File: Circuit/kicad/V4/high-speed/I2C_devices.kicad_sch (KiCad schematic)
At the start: 77 parts, among them U15 LSF0108PWR, U16 TCA9548APWR, U27 LSF0108PWR, U28 TCA9548APWR

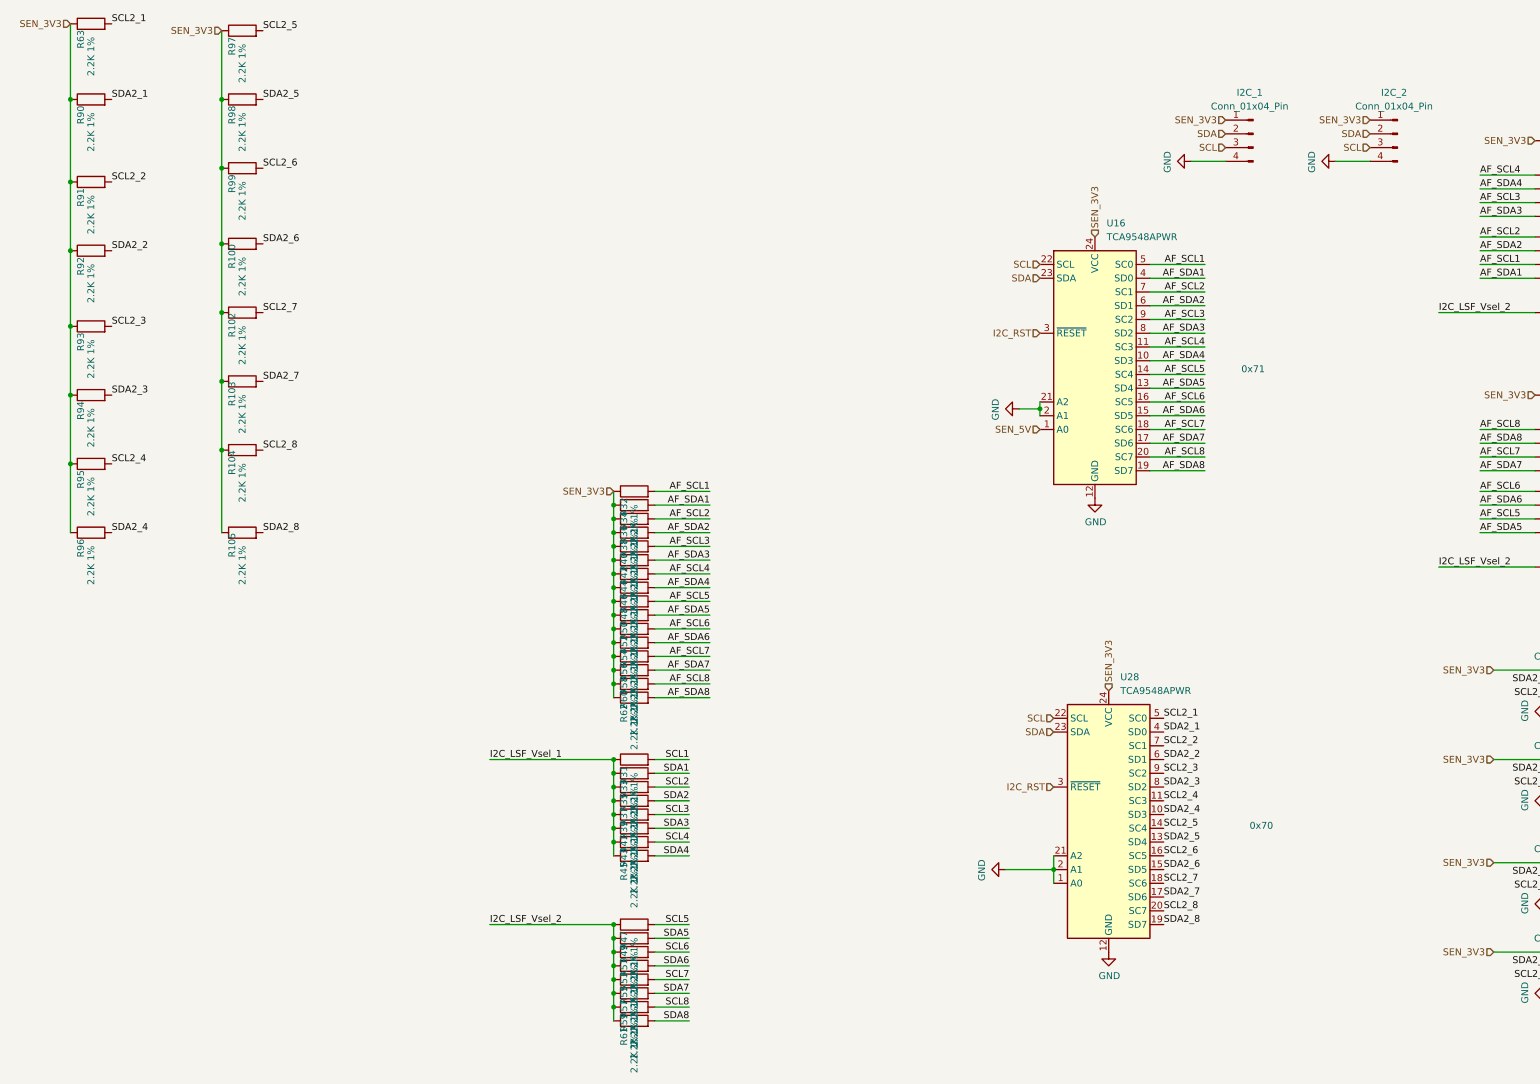
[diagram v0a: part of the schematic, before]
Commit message: added psu start delay rc tag, high speed first inner and outboard impedance calculations
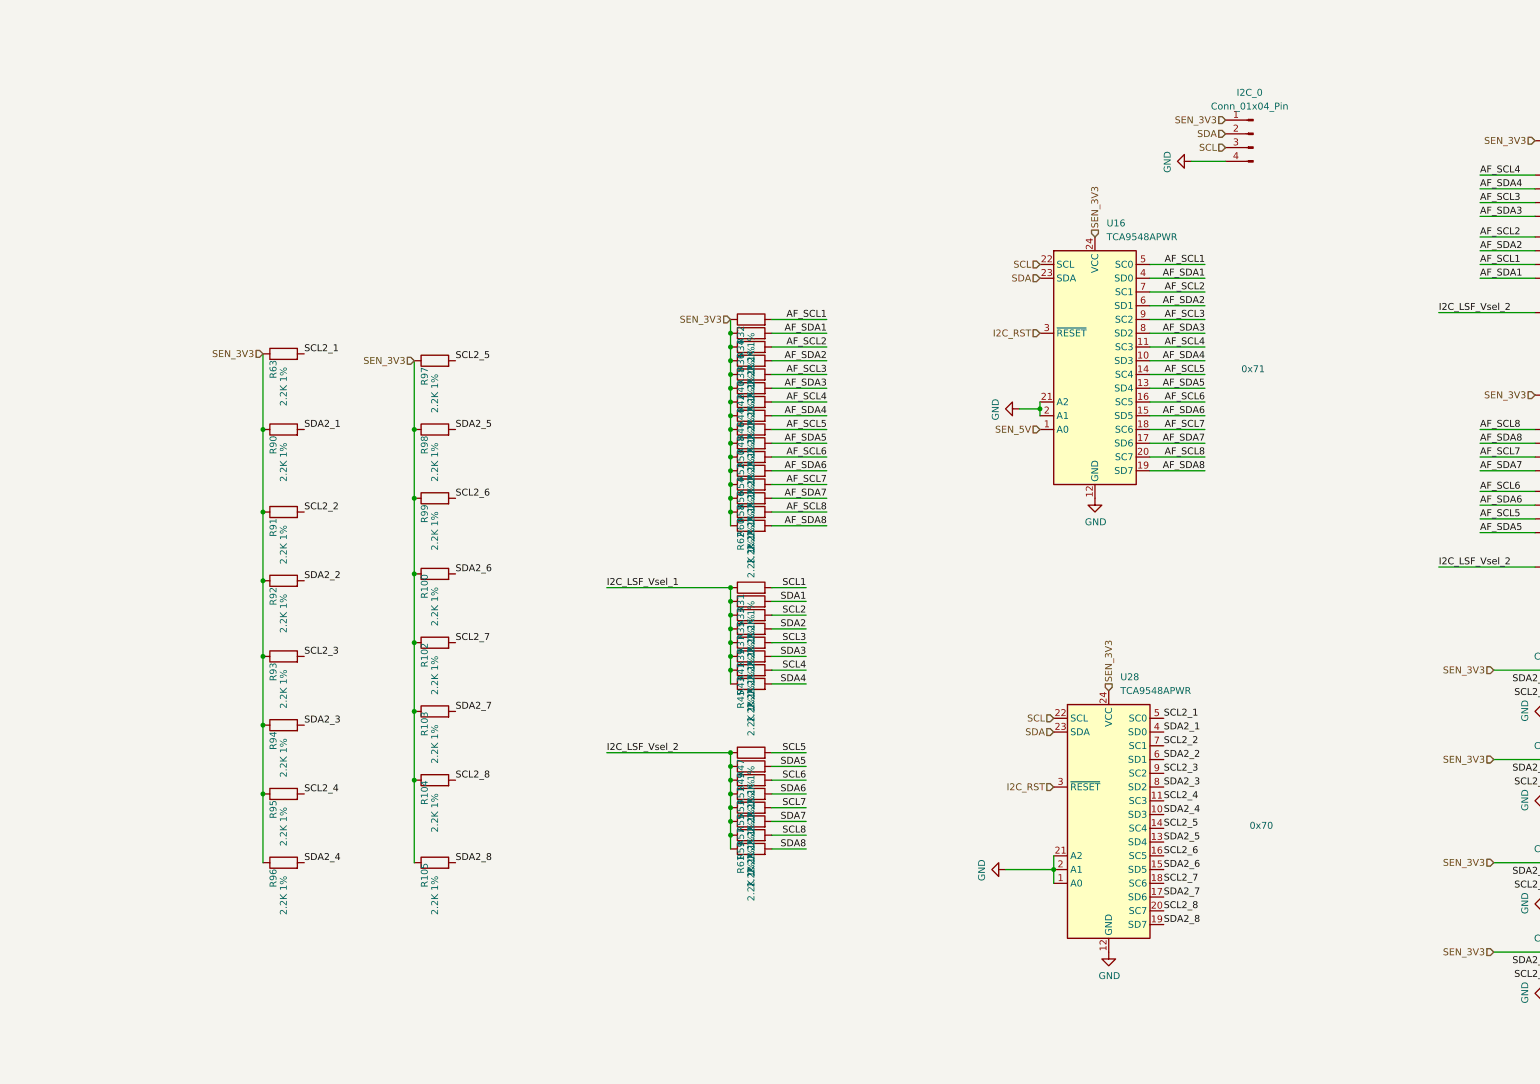
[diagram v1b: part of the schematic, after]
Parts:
- removed I2C_1, I2C_2: Conn_01x04_Pin, Connector_JST:JST_PH_B4B-PH-K_1x04_P2.00mm_Vertical, symbol Connector:Conn_01x04_Pin
- added I2C_0: Conn_01x04_Pin, Connector_JST:JST_SH_BM04B-SRSS-TB_1x04-1MP_P1.00mm_Vertical, symbol Connector:Conn_01x04_Pin
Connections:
- net GND: now also I2C_0.4 (Pin_4)
- net SCL: now also I2C_0.3 (Pin_3)
- net SDA: now also I2C_0.2 (Pin_2)
- net SEN_3V3: now also I2C_0.1 (Pin_1)
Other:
- moved on the sheet: R100, R102, R103, R104, R105, R31, R32, R33, R34, R35, R36, R37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

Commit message: kicad: high speed V2.2 Circuit finish psu bom update
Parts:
- added R64, R75: 2.2K, Capacitor_SMD:C_0603_1608Metric, symbol Device:R
- C32: renamed from C26; Cikkszám (none) -> 100.277.53; Link (none) -> https://www.hestore.hu/prod_10027753.html
- C33: renamed from C27; Cikkszám (none) -> 100.277.53; Link (none) -> https://www.hestore.hu/prod_10027753.html
- C34: renamed from C28; Cikkszám (none) -> 100.277.53; Link (none) -> https://www.hestore.hu/prod_10027753.html
- CT6: renamed from CT4; value 10uf -> 10uF; Cikkszám (none) -> 100.230.37; Link (none) -> https://www.hestore.hu/prod_10023037.html
- I2C_0x70_1, I2C_0x70_2, I2C_0x70_3, I2C_0x70_4, I2C_0x70_5, I2C_0x70_6, I2C_0x70_7, I2C_0x70_8, I2C_0x71_1, I2C_0x71_8: Cikkszám (none) -> 100.491.15; Link (none) -> https://www.hestore.hu/prod_10049115.html
- I2C_0x71_2: renamed from I2C_0x71_5; Cikkszám (none) -> 100.491.15; Link (none) -> https://www.hestore.hu/prod_10049115.html
- I2C_0x71_3: renamed from I2C_0x71_2; Cikkszám (none) -> 100.491.15; Link (none) -> https://www.hestore.hu/prod_10049115.html
- I2C_0x71_4: renamed from I2C_0x71_6; Cikkszám (none) -> 100.491.15; Link (none) -> https://www.hestore.hu/prod_10049115.html
- I2C_0x71_5: renamed from I2C_0x71_3; Cikkszám (none) -> 100.491.15; Link (none) -> https://www.hestore.hu/prod_10049115.html
- I2C_0x71_6: renamed from I2C_0x71_7; Cikkszám (none) -> 100.491.15; Link (none) -> https://www.hestore.hu/prod_10049115.html
- I2C_0x71_7: renamed from I2C_0x71_4; Cikkszám (none) -> 100.491.15; Link (none) -> https://www.hestore.hu/prod_10049115.html
- I2C_1: renamed from I2C_0; Cikkszám (none) -> 100.491.15; Link (none) -> https://www.hestore.hu/prod_10049115.html
- R42: renamed from R63; value 2.2K 1% -> 2.2K; footprint Resistor_SMD:R_0805_2012Metric -> Capacitor_SMD:C_0603_1608Metric; Cikkszám (none) -> 100.406.77; Field4 Farnell -> (none); Link (none) -> https://www.hestore.hu/prod_10040677.html; Part Description Resistor 2.2K M1005 1% 63mW -> (none)
- R43: renamed from R97; value 2.2K 1% -> 2.2K; footprint Resistor_SMD:R_0805_2012Metric -> Capacitor_SMD:C_0603_1608Metric; Cikkszám (none) -> 100.406.77; Field4 Farnell -> (none); Link (none) -> https://www.hestore.hu/prod_10040677.html; Part Description Resistor 2.2K M1005 1% 63mW -> (none)
- R44: renamed from R90; value 2.2K 1% -> 2.2K; footprint Resistor_SMD:R_0805_2012Metric -> Capacitor_SMD:C_0603_1608Metric; Cikkszám (none) -> 100.406.77; Field4 Farnell -> (none); Link (none) -> https://www.hestore.hu/prod_10040677.html; Part Description Resistor 2.2K M1005 1% 63mW -> (none)
- R45: renamed from R98; value 2.2K 1% -> 2.2K; footprint Resistor_SMD:R_0805_2012Metric -> Capacitor_SMD:C_0603_1608Metric; Cikkszám (none) -> 100.406.77; Field4 Farnell -> (none); Link (none) -> https://www.hestore.hu/prod_10040677.html; Part Description Resistor 2.2K M1005 1% 63mW -> (none)
- R46: renamed from R99; value 2.2K 1% -> 2.2K; footprint Resistor_SMD:R_0805_2012Metric -> Capacitor_SMD:C_0603_1608Metric; Cikkszám (none) -> 100.406.77; Field4 Farnell -> (none); Link (none) -> https://www.hestore.hu/prod_10040677.html; Part Description Resistor 2.2K M1005 1% 63mW -> (none)
- R47: renamed from R91; value 2.2K 1% -> 2.2K; footprint Resistor_SMD:R_0805_2012Metric -> Capacitor_SMD:C_0603_1608Metric; Cikkszám (none) -> 100.406.77; Field4 Farnell -> (none); Link (none) -> https://www.hestore.hu/prod_10040677.html; Part Description Resistor 2.2K M1005 1% 63mW -> (none)
- R48: renamed from R100; value 2.2K 1% -> 2.2K; footprint Resistor_SMD:R_0805_2012Metric -> Capacitor_SMD:C_0603_1608Metric; Cikkszám (none) -> 100.406.77; Field4 Farnell -> (none); Link (none) -> https://www.hestore.hu/prod_10040677.html; Part Description Resistor 2.2K M1005 1% 63mW -> (none)
- R49: renamed from R92; value 2.2K 1% -> 2.2K; footprint Resistor_SMD:R_0805_2012Metric -> Capacitor_SMD:C_0603_1608Metric; Cikkszám (none) -> 100.406.77; Field4 Farnell -> (none); Link (none) -> https://www.hestore.hu/prod_10040677.html; Part Description Resistor 2.2K M1005 1% 63mW -> (none)
- R50: renamed from R102; value 2.2K 1% -> 2.2K; footprint Resistor_SMD:R_0805_2012Metric -> Capacitor_SMD:C_0603_1608Metric; Cikkszám (none) -> 100.406.77; Field4 Farnell -> (none); Link (none) -> https://www.hestore.hu/prod_10040677.html; Part Description Resistor 2.2K M1005 1% 63mW -> (none)
- R51: renamed from R93; value 2.2K 1% -> 2.2K; footprint Resistor_SMD:R_0805_2012Metric -> Capacitor_SMD:C_0603_1608Metric; Cikkszám (none) -> 100.406.77; Field4 Farnell -> (none); Link (none) -> https://www.hestore.hu/prod_10040677.html; Part Description Resistor 2.2K M1005 1% 63mW -> (none)
- R52: renamed from R103; value 2.2K 1% -> 2.2K; footprint Resistor_SMD:R_0805_2012Metric -> Capacitor_SMD:C_0603_1608Metric; Cikkszám (none) -> 100.406.77; Field4 Farnell -> (none); Link (none) -> https://www.hestore.hu/prod_10040677.html; Part Description Resistor 2.2K M1005 1% 63mW -> (none)
- R53: renamed from R94; value 2.2K 1% -> 2.2K; footprint Resistor_SMD:R_0805_2012Metric -> Capacitor_SMD:C_0603_1608Metric; Cikkszám (none) -> 100.406.77; Field4 Farnell -> (none); Link (none) -> https://www.hestore.hu/prod_10040677.html; Part Description Resistor 2.2K M1005 1% 63mW -> (none)
- R54: renamed from R31; value 2.2K 1% -> 2.2K; footprint Resistor_SMD:R_0805_2012Metric -> Capacitor_SMD:C_0603_1608Metric; Cikkszám (none) -> 100.406.77; Field4 Farnell -> (none); Link (none) -> https://www.hestore.hu/prod_10040677.html; Part Description Resistor 2.2K M1005 1% 63mW -> (none)
- R55: renamed from R47; value 2.2K 1% -> 2.2K; footprint Resistor_SMD:R_0805_2012Metric -> Capacitor_SMD:C_0603_1608Metric; Cikkszám (none) -> 100.406.77; Field4 Farnell -> (none); Link (none) -> https://www.hestore.hu/prod_10040677.html; Part Description Resistor 2.2K M1005 1% 63mW -> (none)
- R56: renamed from R33; value 2.2K 1% -> 2.2K; footprint Resistor_SMD:R_0805_2012Metric -> Capacitor_SMD:C_0603_1608Metric; Cikkszám (none) -> 100.406.77; Field4 Farnell -> (none); Link (none) -> https://www.hestore.hu/prod_10040677.html; Part Description Resistor 2.2K M1005 1% 63mW -> (none)
- R57: renamed from R49; value 2.2K 1% -> 2.2K; footprint Resistor_SMD:R_0805_2012Metric -> Capacitor_SMD:C_0603_1608Metric; Cikkszám (none) -> 100.406.77; Field4 Farnell -> (none); Link (none) -> https://www.hestore.hu/prod_10040677.html; Part Description Resistor 2.2K M1005 1% 63mW -> (none)
- R58: renamed from R35; value 2.2K 1% -> 2.2K; footprint Resistor_SMD:R_0805_2012Metric -> Capacitor_SMD:C_0603_1608Metric; Cikkszám (none) -> 100.406.77; Field4 Farnell -> (none); Link (none) -> https://www.hestore.hu/prod_10040677.html; Part Description Resistor 2.2K M1005 1% 63mW -> (none)
- R59: renamed from R51; value 2.2K 1% -> 2.2K; footprint Resistor_SMD:R_0805_2012Metric -> Capacitor_SMD:C_0603_1608Metric; Cikkszám (none) -> 100.406.77; Field4 Farnell -> (none); Link (none) -> https://www.hestore.hu/prod_10040677.html; Part Description Resistor 2.2K M1005 1% 63mW -> (none)
- R60: renamed from R104; value 2.2K 1% -> 2.2K; footprint Resistor_SMD:R_0805_2012Metric -> Capacitor_SMD:C_0603_1608Metric; Cikkszám (none) -> 100.406.77; Field4 Farnell -> (none); Link (none) -> https://www.hestore.hu/prod_10040677.html; Part Description Resistor 2.2K M1005 1% 63mW -> (none)
- R61: renamed from R37; value 2.2K 1% -> 2.2K; footprint Resistor_SMD:R_0805_2012Metric -> Capacitor_SMD:C_0603_1608Metric; Cikkszám (none) -> 100.406.77; Field4 Farnell -> (none); Link (none) -> https://www.hestore.hu/prod_10040677.html; Part Description Resistor 2.2K M1005 1% 63mW -> (none)
- R62: renamed from R53; value 2.2K 1% -> 2.2K; footprint Resistor_SMD:R_0805_2012Metric -> Capacitor_SMD:C_0603_1608Metric; Cikkszám (none) -> 100.406.77; Field4 Farnell -> (none); Link (none) -> https://www.hestore.hu/prod_10040677.html; Part Description Resistor 2.2K M1005 1% 63mW -> (none)
- R63: renamed from R95; value 2.2K 1% -> 2.2K; footprint Resistor_SMD:R_0805_2012Metric -> Capacitor_SMD:C_0603_1608Metric; Cikkszám (none) -> 100.406.77; Field4 Farnell -> (none); Link (none) -> https://www.hestore.hu/prod_10040677.html; Part Description Resistor 2.2K M1005 1% 63mW -> (none)
- R65: renamed from R39; value 2.2K 1% -> 2.2K; footprint Resistor_SMD:R_0805_2012Metric -> Capacitor_SMD:C_0603_1608Metric; Cikkszám (none) -> 100.406.77; Field4 Farnell -> (none); Link (none) -> https://www.hestore.hu/prod_10040677.html; Part Description Resistor 2.2K M1005 1% 63mW -> (none)
- R66: renamed from R55; value 2.2K 1% -> 2.2K; footprint Resistor_SMD:R_0805_2012Metric -> Capacitor_SMD:C_0603_1608Metric; Cikkszám (none) -> 100.406.77; Field4 Farnell -> (none); Link (none) -> https://www.hestore.hu/prod_10040677.html; Part Description Resistor 2.2K M1005 1% 63mW -> (none)
- R67: renamed from R41; value 2.2K 1% -> 2.2K; footprint Resistor_SMD:R_0805_2012Metric -> Capacitor_SMD:C_0603_1608Metric; Cikkszám (none) -> 100.406.77; Field4 Farnell -> (none); Link (none) -> https://www.hestore.hu/prod_10040677.html; Part Description Resistor 2.2K M1005 1% 63mW -> (none)
- R68: renamed from R57; value 2.2K 1% -> 2.2K; footprint Resistor_SMD:R_0805_2012Metric -> Capacitor_SMD:C_0603_1608Metric; Cikkszám (none) -> 100.406.77; Field4 Farnell -> (none); Link (none) -> https://www.hestore.hu/prod_10040677.html; Part Description Resistor 2.2K M1005 1% 63mW -> (none)
- R69: renamed from R43; value 2.2K 1% -> 2.2K; footprint Resistor_SMD:R_0805_2012Metric -> Capacitor_SMD:C_0603_1608Metric; Cikkszám (none) -> 100.406.77; Field4 Farnell -> (none); Link (none) -> https://www.hestore.hu/prod_10040677.html; Part Description Resistor 2.2K M1005 1% 63mW -> (none)
- R70: renamed from R59; value 2.2K 1% -> 2.2K; footprint Resistor_SMD:R_0805_2012Metric -> Capacitor_SMD:C_0603_1608Metric; Cikkszám (none) -> 100.406.77; Field4 Farnell -> (none); Link (none) -> https://www.hestore.hu/prod_10040677.html; Part Description Resistor 2.2K M1005 1% 63mW -> (none)
- R71: renamed from R45; value 2.2K 1% -> 2.2K; footprint Resistor_SMD:R_0805_2012Metric -> Capacitor_SMD:C_0603_1608Metric; Cikkszám (none) -> 100.406.77; Field4 Farnell -> (none); Link (none) -> https://www.hestore.hu/prod_10040677.html; Part Description Resistor 2.2K M1005 1% 63mW -> (none)
- R72: renamed from R61; value 2.2K 1% -> 2.2K; footprint Resistor_SMD:R_0805_2012Metric -> Capacitor_SMD:C_0603_1608Metric; Cikkszám (none) -> 100.406.77; Field4 Farnell -> (none); Link (none) -> https://www.hestore.hu/prod_10040677.html; Part Description Resistor 2.2K M1005 1% 63mW -> (none)
- R73: renamed from R96; value 2.2K 1% -> 2.2K; footprint Resistor_SMD:R_0805_2012Metric -> Capacitor_SMD:C_0603_1608Metric; Cikkszám (none) -> 100.406.77; Field4 Farnell -> (none); Link (none) -> https://www.hestore.hu/prod_10040677.html; Part Description Resistor 2.2K M1005 1% 63mW -> (none)
- R74: renamed from R105; value 2.2K 1% -> 2.2K; footprint Resistor_SMD:R_0805_2012Metric -> Capacitor_SMD:C_0603_1608Metric; Cikkszám (none) -> 100.406.77; Field4 Farnell -> (none); Link (none) -> https://www.hestore.hu/prod_10040677.html; Part Description Resistor 2.2K M1005 1% 63mW -> (none)
- R76: renamed from R32; value 2.2K 1% -> 2.2K; footprint Resistor_SMD:R_0805_2012Metric -> Capacitor_SMD:C_0603_1608Metric; Cikkszám (none) -> 100.406.77; Field4 Farnell -> (none); Link (none) -> https://www.hestore.hu/prod_10040677.html; Part Description Resistor 2.2K M1005 1% 63mW -> (none)
- R77: renamed from R34; value 2.2K 1% -> 2.2K; footprint Resistor_SMD:R_0805_2012Metric -> Capacitor_SMD:C_0603_1608Metric; Cikkszám (none) -> 100.406.77; Field4 Farnell -> (none); Link (none) -> https://www.hestore.hu/prod_10040677.html; Part Description Resistor 2.2K M1005 1% 63mW -> (none)
- R78: renamed from R36; value 2.2K 1% -> 2.2K; footprint Resistor_SMD:R_0805_2012Metric -> Capacitor_SMD:C_0603_1608Metric; Cikkszám (none) -> 100.406.77; Field4 Farnell -> (none); Link (none) -> https://www.hestore.hu/prod_10040677.html; Part Description Resistor 2.2K M1005 1% 63mW -> (none)
- R79: renamed from R38; value 2.2K 1% -> 2.2K; footprint Resistor_SMD:R_0805_2012Metric -> Capacitor_SMD:C_0603_1608Metric; Cikkszám (none) -> 100.406.77; Field4 Farnell -> (none); Link (none) -> https://www.hestore.hu/prod_10040677.html; Part Description Resistor 2.2K M1005 1% 63mW -> (none)
- R80: renamed from R40; value 2.2K 1% -> 2.2K; footprint Resistor_SMD:R_0805_2012Metric -> Capacitor_SMD:C_0603_1608Metric; Cikkszám (none) -> 100.406.77; Field4 Farnell -> (none); Link (none) -> https://www.hestore.hu/prod_10040677.html; Part Description Resistor 2.2K M1005 1% 63mW -> (none)
- R81: renamed from R42; value 2.2K 1% -> 2.2K; footprint Resistor_SMD:R_0805_2012Metric -> Capacitor_SMD:C_0603_1608Metric; Cikkszám (none) -> 100.406.77; Field4 Farnell -> (none); Link (none) -> https://www.hestore.hu/prod_10040677.html; Part Description Resistor 2.2K M1005 1% 63mW -> (none)
- R82: renamed from R44; value 2.2K 1% -> 2.2K; footprint Resistor_SMD:R_0805_2012Metric -> Capacitor_SMD:C_0603_1608Metric; Cikkszám (none) -> 100.406.77; Field4 Farnell -> (none); Link (none) -> https://www.hestore.hu/prod_10040677.html; Part Description Resistor 2.2K M1005 1% 63mW -> (none)
- R83: renamed from R46; value 2.2K 1% -> 2.2K; footprint Resistor_SMD:R_0805_2012Metric -> Capacitor_SMD:C_0603_1608Metric; Cikkszám (none) -> 100.406.77; Field4 Farnell -> (none); Link (none) -> https://www.hestore.hu/prod_10040677.html; Part Description Resistor 2.2K M1005 1% 63mW -> (none)
- R84: renamed from R48; value 2.2K 1% -> 2.2K; footprint Resistor_SMD:R_0805_2012Metric -> Capacitor_SMD:C_0603_1608Metric; Cikkszám (none) -> 100.406.77; Field4 Farnell -> (none); Link (none) -> https://www.hestore.hu/prod_10040677.html; Part Description Resistor 2.2K M1005 1% 63mW -> (none)
- R85: renamed from R101; value 10k -> 10K; Cikkszám (none) -> 100.011.45; Link (none) -> https://www.hestore.hu/prod_10001145.html
- R86: renamed from R50; value 2.2K 1% -> 2.2K; footprint Resistor_SMD:R_0805_2012Metric -> Capacitor_SMD:C_0603_1608Metric; Cikkszám (none) -> 100.406.77; Field4 Farnell -> (none); Link (none) -> https://www.hestore.hu/prod_10040677.html; Part Description Resistor 2.2K M1005 1% 63mW -> (none)
- R87: renamed from R52; value 2.2K 1% -> 2.2K; footprint Resistor_SMD:R_0805_2012Metric -> Capacitor_SMD:C_0603_1608Metric; Cikkszám (none) -> 100.406.77; Field4 Farnell -> (none); Link (none) -> https://www.hestore.hu/prod_10040677.html; Part Description Resistor 2.2K M1005 1% 63mW -> (none)
- R88: renamed from R54; value 2.2K 1% -> 2.2K; footprint Resistor_SMD:R_0805_2012Metric -> Capacitor_SMD:C_0603_1608Metric; Cikkszám (none) -> 100.406.77; Field4 Farnell -> (none); Link (none) -> https://www.hestore.hu/prod_10040677.html; Part Description Resistor 2.2K M1005 1% 63mW -> (none)
- R89: renamed from R56; value 2.2K 1% -> 2.2K; footprint Resistor_SMD:R_0805_2012Metric -> Capacitor_SMD:C_0603_1608Metric; Cikkszám (none) -> 100.406.77; Field4 Farnell -> (none); Link (none) -> https://www.hestore.hu/prod_10040677.html; Part Description Resistor 2.2K M1005 1% 63mW -> (none)
- R90: renamed from R58; value 2.2K 1% -> 2.2K; footprint Resistor_SMD:R_0805_2012Metric -> Capacitor_SMD:C_0603_1608Metric; Cikkszám (none) -> 100.406.77; Field4 Farnell -> (none); Link (none) -> https://www.hestore.hu/prod_10040677.html; Part Description Resistor 2.2K M1005 1% 63mW -> (none)
- R91: renamed from R60; value 2.2K 1% -> 2.2K; footprint Resistor_SMD:R_0805_2012Metric -> Capacitor_SMD:C_0603_1608Metric; Cikkszám (none) -> 100.406.77; Field4 Farnell -> (none); Link (none) -> https://www.hestore.hu/prod_10040677.html; Part Description Resistor 2.2K M1005 1% 63mW -> (none)
- R92: renamed from R62; value 2.2K 1% -> 2.2K; footprint Resistor_SMD:R_0805_2012Metric -> Capacitor_SMD:C_0603_1608Metric; Cikkszám (none) -> 100.406.77; Field4 Farnell -> (none); Link (none) -> https://www.hestore.hu/prod_10040677.html; Part Description Resistor 2.2K M1005 1% 63mW -> (none)
- U15: footprint psu:SOP65P640X120-20N -> panel:SOP65P640X120-20N; Availability In Stock -> (none); Check_prices https://www.snapeda.com/parts/LSF0108PWR/Texas+Instruments/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 -> (none); Cikkszám (none) -> 100.403.41; Description_1 Octal bidirectional multi-voltage-level translator -> (none); Link (none) -> https://www.hestore.hu/prod_10040341.html; MF Texas Instruments -> (none); MP LSF0108PWR -> (none); Package TSSOP-20 Texas Instruments -> (none); Price None -> (none); SnapEDA_Link https://www.snapeda.com/parts/LSF0108PWR/Texas+Instruments/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 -> (none)
- U16: Cikkszám (none) -> 100.433.42; Link (none) -> https://www.hestore.hu/prod_10043342.html
- U17: renamed from U27; footprint psu:SOP65P640X120-20N -> panel:SOP65P640X120-20N; Availability In Stock -> (none); Check_prices https://www.snapeda.com/parts/LSF0108PWR/Texas+Instruments/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 -> (none); Cikkszám (none) -> 100.403.41; Description_1 Octal bidirectional multi-voltage-level translator -> (none); Link (none) -> https://www.hestore.hu/prod_10040341.html; MF Texas Instruments -> (none); MP LSF0108PWR -> (none); Package TSSOP-20 Texas Instruments -> (none); Price None -> (none); SnapEDA_Link https://www.snapeda.com/parts/LSF0108PWR/Texas+Instruments/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 -> (none)
- U18: renamed from U28; Cikkszám (none) -> 100.433.42; Link (none) -> https://www.hestore.hu/prod_10043342.html
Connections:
- net SCL: now also R75.2
- net SDA: now also R64.2
- net SEN_3V3: now also R64.1, R75.1
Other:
- moved on the sheet: I2C_0x70_1, I2C_0x70_2, I2C_0x70_3, I2C_0x70_4, I2C_0x70_5, I2C_0x70_6, I2C_0x70_7, I2C_0x70_8, I2C_0x71_1, I2C_0x71_2, I2C_0x71_3, I2C_0x71_4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
